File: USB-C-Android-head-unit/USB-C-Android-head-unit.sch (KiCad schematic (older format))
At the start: 0 parts

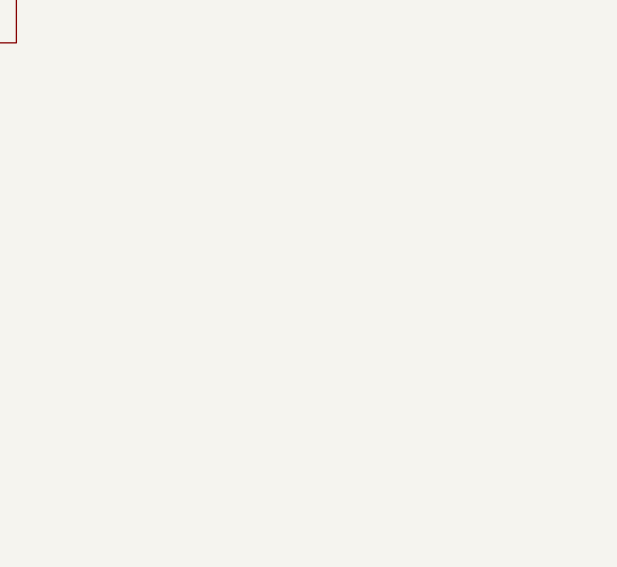
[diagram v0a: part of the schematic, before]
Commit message: starting usb c design
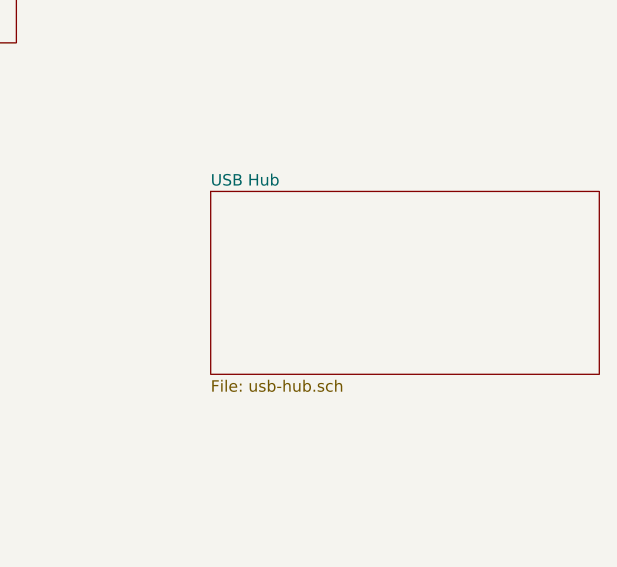
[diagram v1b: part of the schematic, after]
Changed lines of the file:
@@
 EESchema Schematic File Version 4
+LIBS:USB-C-Android-head-unit-cache
 EELAYER 30 0
 EELAYER END
 $Descr USLetter 11000 8500
 encoding utf-8
-Sheet 1 5
+Sheet 1 7
 Title "Master Sheet"
 Date ""
@@
 F1 "audio.sch" 50
 $EndSheet
+$Sheet
+S 9700 3500 1700 800
+U 5DE50791
+F0 "USB Hub" 50
+F1 "usb-hub.sch" 50
+$EndSheet
 $EndSCHEMATC
